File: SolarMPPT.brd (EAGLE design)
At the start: 73.7 x 43.2 mm, 47 parts, among them J1 CORTEX_DEBUG_SMD, J2 1X2-3.5MM, J3 1X2-3.5MM, J4 1X2-3.5MM, J5 1X2-3.5MM, J6 1X2-3.5MM, U1 STM32F091CCT6, U3 LTC1155, U6 3.3V, U7 LM22674MRX-5.0

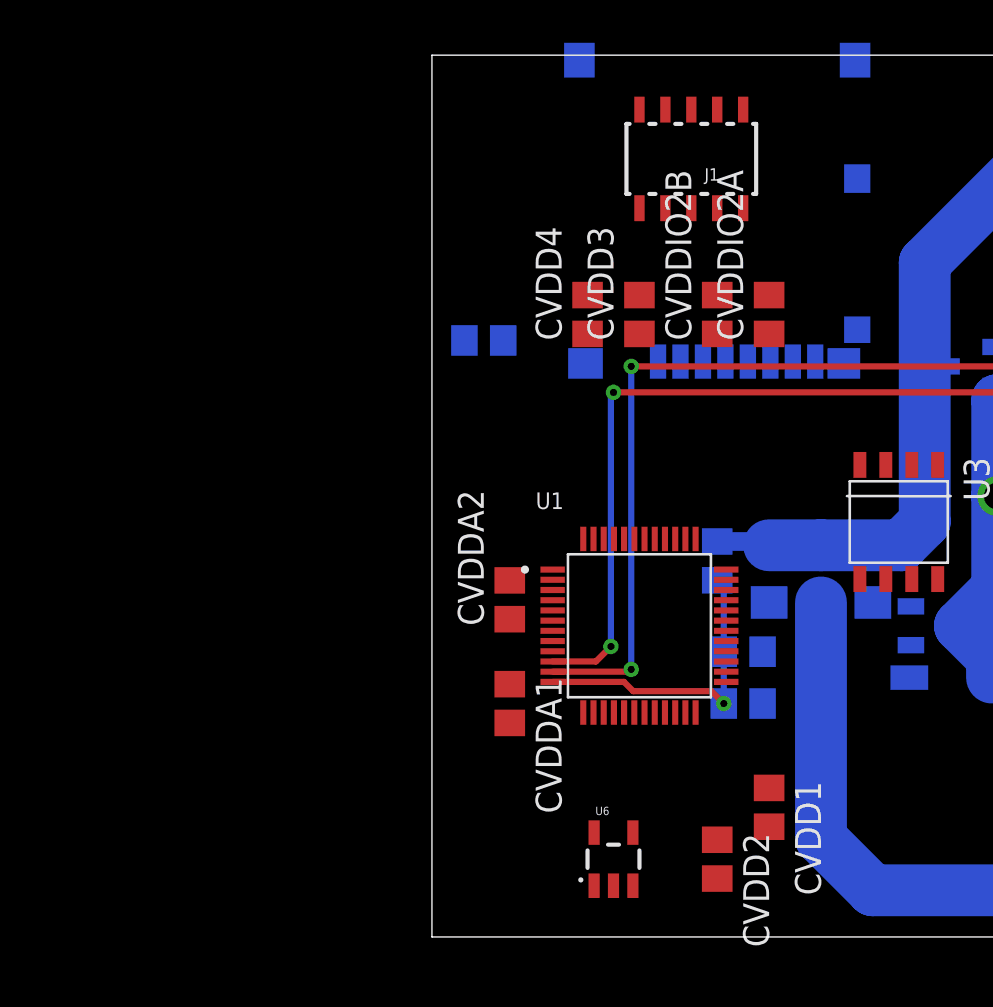
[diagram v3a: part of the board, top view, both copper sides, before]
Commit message: removed 3.3v regulator (using teensy onboard)
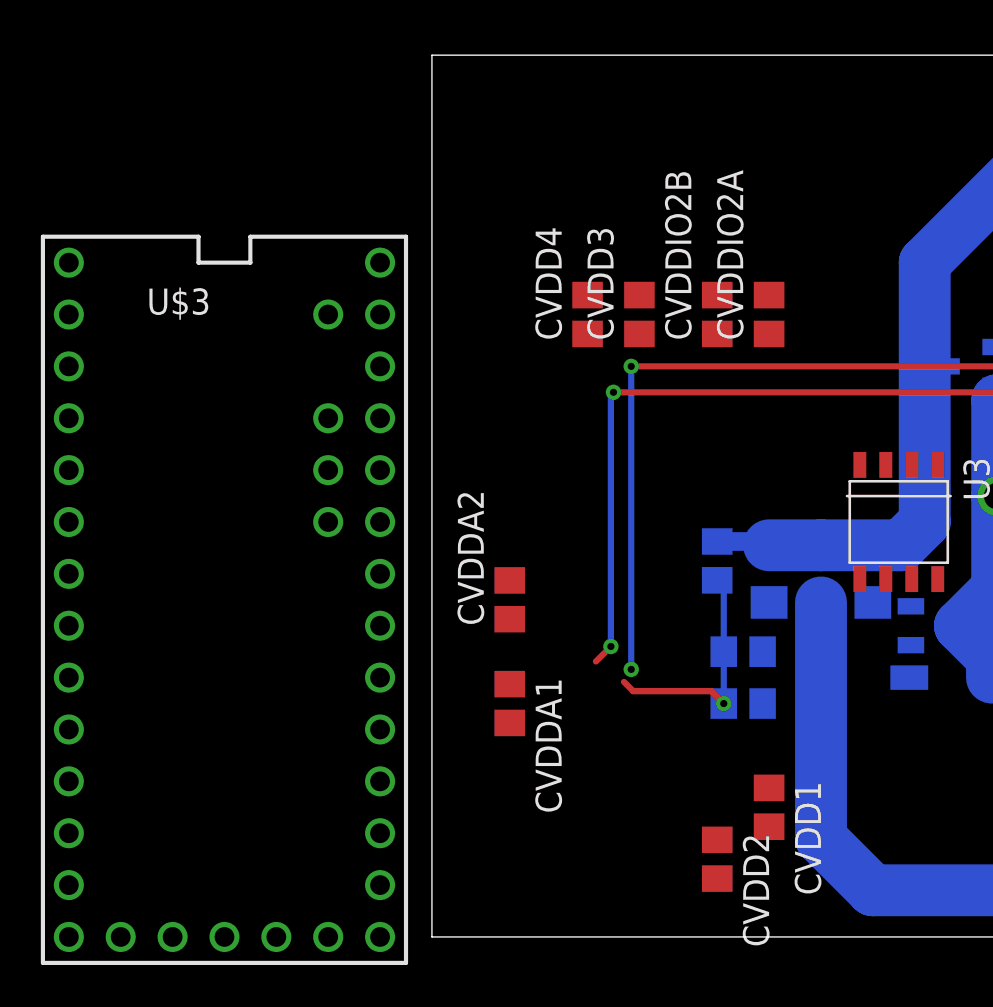
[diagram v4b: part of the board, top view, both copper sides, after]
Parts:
- removed CSD: 1uF, rcl:C0805
- removed H1: MOLEX-502744, FormE:MOLEX-502774
- removed J1: CORTEX_DEBUG_SMD, SparkFun-Connectors:SAMTECH_FTSH-105-01
- removed U1: STM32F091CCT6, Microcontroller:LQFP-48
- removed U6: 3.3V, SparkFun-IC-Power:SOT23-5
- added U$3: TEENSY_3.1+4, FormE:TEENSY_3.1+4
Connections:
- removed net !RESET: J1.10, U1.7
- removed net CS0: H1.2, U1.14
- removed net MISO: H1.7, U1.16
- removed net MOSI: H1.3, U1.17
- removed net N$1: J1.4, U1.37
- removed net N$2: J1.2, U1.34
- removed net SCLK: H1.5, U1.15
- new net 3.3V: U$3.3.3V, U$3.3.3V1
- new net AGND: U$3.AGND
- new net AREF: U$3.AREF
- new net VBAT: U$3.VBAT
- new net VIN: U$3.VIN
- new net VUSB: U$3.VUSB
- net +3V3: no longer CSD.1, H1.4, J1.1, U1.1, U1.24, U1.36, U1.48, U1.9, U6.5
- net +5V: no longer U6.1, U6.3
- net BATT_SENS: no longer U1.11
- net CURR_SENS: no longer U1.10
- net GND: now also U$3.GND, U$3.GND1; no longer CSD.2, H1.6, H1.SH1, H1.SH2, H1.SH3, H1.SH4, J1.3, J1.5, J1.9, U1.23, U1.35, U1.47, U1.8, U6.2
- net SOLAR_SENS: no longer U1.12
- net TIME_OUT: no longer U1.29
- net TIME_OUTN: no longer U1.26
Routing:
- net BATT_SENS: track 46.1 -> 42.4 mm
- net SOLAR_SENS: track 15.0 -> 11.5 mm
- net CURR_SENS: track 48.9 -> 46.8 mm

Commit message: routed!
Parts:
- removed CVDD1, CVDDIO2B: 100nF, rcl:C0805
- removed CVDD2, CVDDIO2A: 4.7uF, rcl:C0805
- removed CVDDA1: 1uF, rcl:C0805
- removed CVDDA2: 10nF, rcl:C0805
- removed J4, J5: 1X2-3.5MM, adafruit:1X2-3.5MM
- added JP1: (no value), pinhead:1X13
- U$3: value TEENSY_3.1+4 -> TEENSY_3.1_BASIC; device FormE:TEENSY_3.1+4 -> FormE:TEENSY_3.1_BASIC
- moved CIN1 58.3 mm to (73.7, 38.1), turned to 90 degrees
- moved CIN3 53.5 mm to (66.0, 38.1), turned to 90 degrees
- moved CIN2 52.4 mm to (69.8, 38.1), turned to 90 degrees
- moved U$3 31.4 mm to (20.3, 22.9)
- moved CVDD3 16.1 mm to (25.4, 35.6)
- moved CVDD4 16.1 mm to (22.9, 35.6)
- moved CSFIL 12.6 mm to (24.1, 22.9), flipped to the top, turned to 0 degrees
- moved RSFIL1 11.0 mm to (24.8, 20.3), flipped to the top, turned to 0 degrees
- moved RSFIL2 10.9 mm to (24.1, 17.8), flipped to the top, turned to 180 degrees
- moved J2 10.2 mm to (80.0, 29.2)
- moved J3 10.2 mm to (80.0, 21.6)
- moved J6 10.2 mm to (80.0, 38.1)
- moved BIGBOB 10.2 mm to (53.3, 21.6)
- moved CCFIL1 10.2 mm to (55.9, 31.8)
- moved CCUR1 10.2 mm to (52.1, 26.7)
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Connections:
- removed net 3.3V: U$3.3.3V, U$3.3.3V1
- removed net AGND: U$3.AGND
- removed net AREF: U$3.AREF
- removed net VIN: U$3.VIN
- removed net VUSB: U$3.VUSB
- new net 3V3B: JP1.2
- new net BUSY: JP1.12, U$3.9
- new net D/C: JP1.8, U$3.5
- new net ECS: JP1.7, U$3.4
- new net ENA: JP1.13, U$3.10
- new net MISO: JP1.5, U$3.12
- new net MOSI: JP1.6, U$3.11
- new net RST: JP1.11, U$3.8
- new net SCLK: JP1.4, U$3.13
- new net SDCS: JP1.10, U$3.7
- new net SRCS: JP1.9, U$3.6
- net +12V: no longer J2.1, J3.1
- net +18V: now also J6.2; no longer J6.1
- net +3V3: now also U$3.3.3V, U$3.3.3V1; no longer CVDD1.1, CVDD2.1, CVDDA1.1, CVDDA2.1, CVDDIO2A.1, CVDDIO2B.1
- net +5V: now also JP1.1, U$3.VIN
- net BATT_SENS: now also U$3.15/A1
- net CURR_SENS: now also U$3.16/A2
- net GND: now also J2.1, J3.1, J6.1, JP1.3, U$3.AGND; no longer CVDD1.2, CVDD2.2, CVDDA1.2, CVDDA2.2, CVDDIO2A.2, CVDDIO2B.2, J4.1, J4.2, J5.1, J5.2, J6.2
- net SOLAR_SENS: now also U$3.14/A0
- net TIME_OUT: now also U$3.23/A9
- net TIME_OUTN: now also U$3.22/A8
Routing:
- net +5V: track 11.4 -> 92.7 mm, vias 2 -> 3
- net +3V3: track 8.40 -> 69.5 mm, vias 0 -> 2
- net SCLK: track 0.00 -> 54.5 mm, vias 0 -> 2
- net MISO: track 0.00 -> 35.9 mm, vias 0 -> 2
- net MOSI: track 0.00 -> 30.8 mm, vias 0 -> 2
- net N$4: track 0.00 -> 19.2 mm, vias 0 -> 3
- net BATT_SENS: track 42.4 -> 59.1 mm, vias 3 -> 4
- net GND: track 99.9 -> 84.6 mm
- net CURR_SENS: track 46.8 -> 61.8 mm
- net RST: track 0.00 -> 12.3 mm
- net ECS: track 0.00 -> 12.3 mm
- net SRCS: track 0.00 -> 12.3 mm
- net SDCS: track 0.00 -> 12.3 mm
- net ENA: track 0.00 -> 12.3 mm
- net D/C: track 0.00 -> 12.3 mm
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- added copper zone on layer 1, net GND
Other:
- board size 73.7 x 43.2 mm -> 85.1 x 43.2 mm

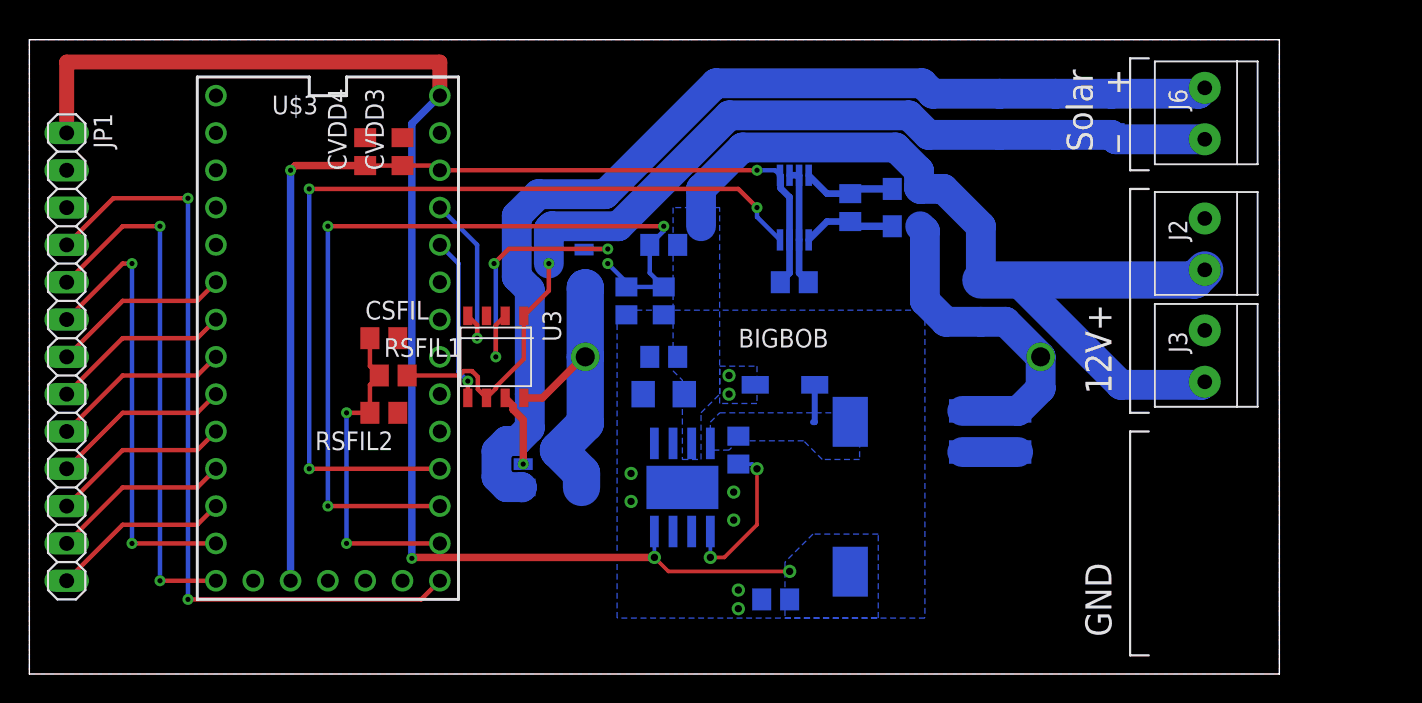
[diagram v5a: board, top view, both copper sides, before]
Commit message: added mounting holes, art, and generally cleaned up before ordering!
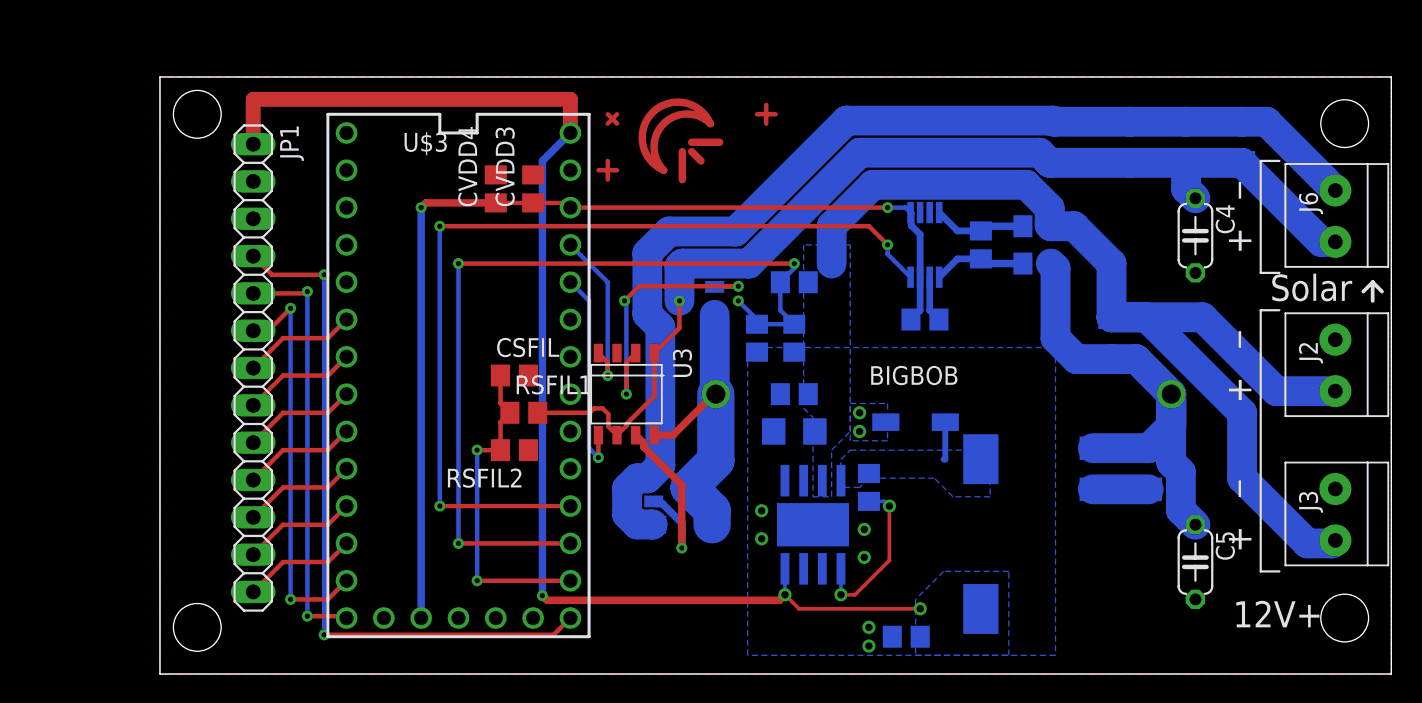
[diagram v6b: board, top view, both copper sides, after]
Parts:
- added C4, C5: (no value), rcl:C050-024X044
- moved J3 14.0 mm to (88.9, 10.8)
- moved JP1 12.7 mm to (15.2, 20.8)
- moved J2 12.1 mm to (88.9, 21.0)
- moved J6 11.3 mm to (88.9, 31.1)
- moved CSFIL 9.25 mm to (33.0, 20.3)
- moved RSFIL2 9.25 mm to (33.0, 15.2)
- moved C1 9.25 mm to (52.1, 19.1)
- moved C2 9.25 mm to (52.1, 16.5)
- moved C3 9.25 mm to (57.1, 12.7)
- moved C6 9.25 mm to (59.7, 2.54)
- moved CBFIL 9.25 mm to (49.5, 22.9)
- moved CCUR1 9.25 mm to (61.0, 24.1)
- moved COUT1 9.25 mm to (76.2, 14.0)
- moved COUT2 9.25 mm to (72.4, 14.0)
- moved CVDD3 9.25 mm to (34.3, 33.0)
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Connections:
- net +18V: now also C4.1
- net GND: now also C4.2, C5.2
- net N$10: now also C5.1
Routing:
- net N$10: track 22.8 -> 32.4 mm
- net N$1: track 0.00 -> 8.98 mm
- net N$8: track 5.02 -> 13.2 mm
- net +12V: track 63.1 -> 70.9 mm
- net SCLK: track 54.5 -> 47.1 mm
- net MISO: track 35.9 -> 28.6 mm
- net +5V: track 92.7 -> 87.4 mm
- net RST: track 12.3 -> 7.72 mm
- net ECS: track 12.3 -> 7.72 mm
- net D/C: track 12.3 -> 7.72 mm
- net BUSY: track 12.3 -> 7.72 mm
- net SRCS: track 12.3 -> 7.72 mm
- net ENA: track 12.3 -> 7.72 mm
- net SDCS: track 12.3 -> 7.72 mm
- net +18V: track 68.5 -> 73.1 mm
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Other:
- board size 85.1 x 43.2 mm -> 83.8 x 40.6 mm
- board text removed: "GND"

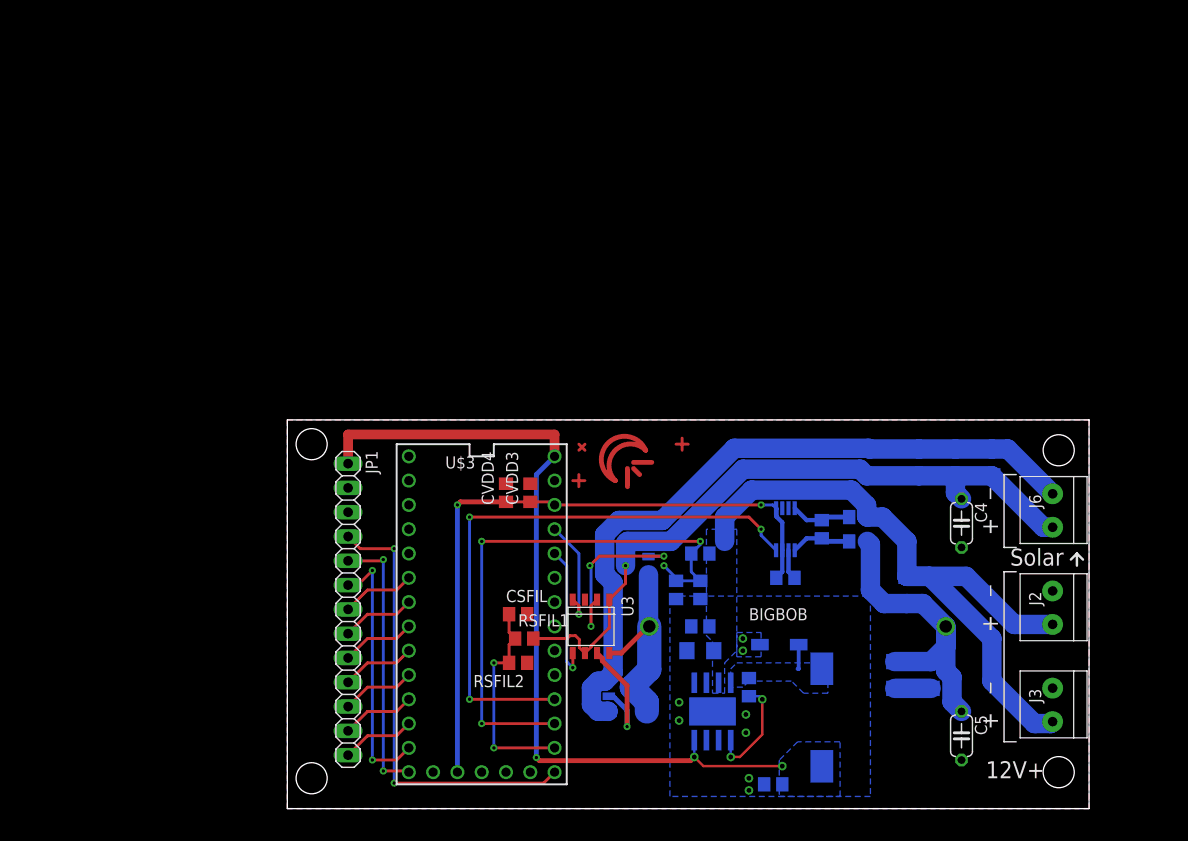
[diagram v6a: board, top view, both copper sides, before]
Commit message: Went back and forth with osh getting it right, this version was ORDERED
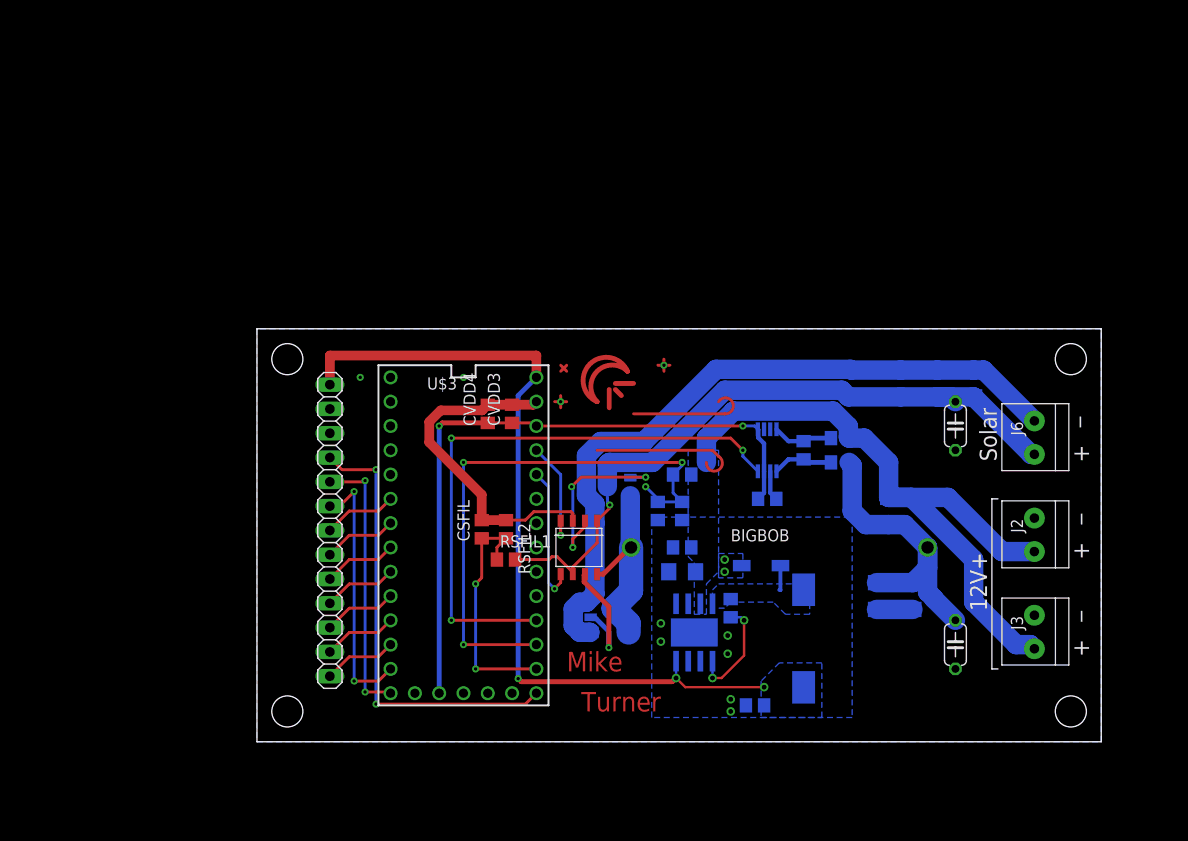
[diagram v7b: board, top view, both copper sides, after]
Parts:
- moved RSFIL2 14.0 mm to (31.8, 29.2), turned to 270 degrees
- moved C4 10.2 mm to (78.7, 40.0)
- moved CSFIL 9.67 mm to (29.2, 29.2), turned to 90 degrees
- moved C5 9.55 mm to (78.7, 17.1)
- moved CIN1 8.47 mm to (80.6, 44.5)
- moved CIN2 8.47 mm to (76.8, 44.5)
- moved CIN3 8.47 mm to (73.0, 44.5)
- moved U$1 8.47 mm to (43.8, 33.7)
- moved U2 8.47 mm to (59.1, 37.5)
- moved CCFIL1 8.47 mm to (62.9, 37.5)
- moved COUT1 8.47 mm to (74.3, 22.2)
- moved COUT2 8.47 mm to (70.5, 22.2)
- moved C1 8.47 mm to (50.2, 27.3)
- moved C2 8.47 mm to (50.2, 24.8)
- moved C3 8.47 mm to (55.2, 21.0)
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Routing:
- net GND: track 81.0 -> 116.6 mm, vias 8 -> 9
- net N$18: track 0.00 -> 14.4 mm
- net N$16: track 0.00 -> 10.9 mm
- net N$9: track 3.81 -> 0.00 mm
- net N$69: track 0.00 -> 3.81 mm
- net SOLAR_SENS: track 22.4 -> 25.4 mm
- net N$3: track 1.27 -> 2.54 mm, vias 0 -> 1
- net N$12: track 1.27 -> 2.54 mm, vias 0 -> 1
- net N$13: track 1.27 -> 0.00 mm
- net N$11: track 1.27 -> 0.00 mm
- net N$7: track 21.2 -> 20.4 mm
- net N$10: track 32.4 -> 31.6 mm
- removed copper zone on layer 1, net GND
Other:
- board size 83.8 x 40.6 mm -> 88.3 x 43.2 mm
- board text added: "Mike"
- board text added: "Turner"
